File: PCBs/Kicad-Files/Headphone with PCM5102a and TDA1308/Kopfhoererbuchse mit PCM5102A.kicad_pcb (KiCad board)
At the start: 2 copper layers, 30.9 x 31.3 mm, 36 parts, among them J1 Conn_02x03_Odd_Even, J2 AudioJack3_Dual_Switch, Q1 IRLML6401, U1 PCM5102A, U2 TDA1308

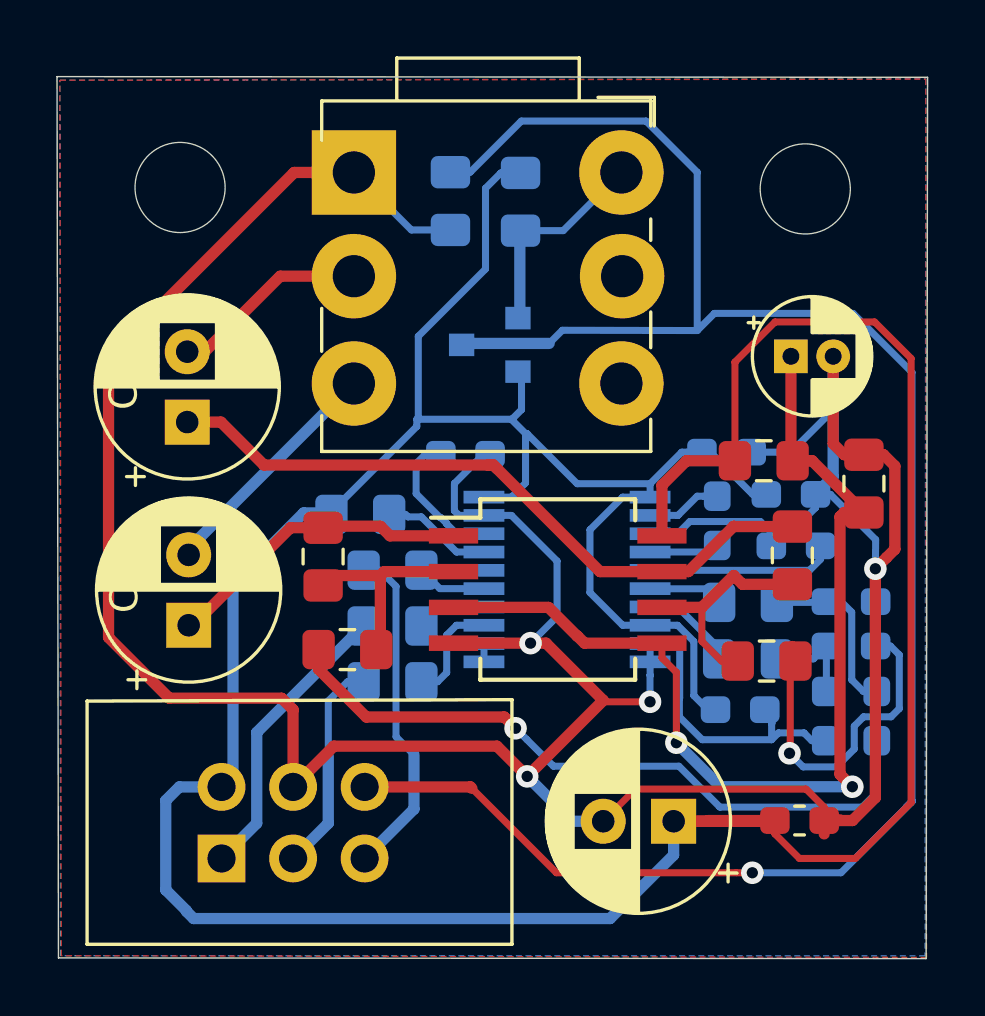
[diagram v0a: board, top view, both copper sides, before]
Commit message: KiCad-Files umbenennen: Kopfhoererplatine
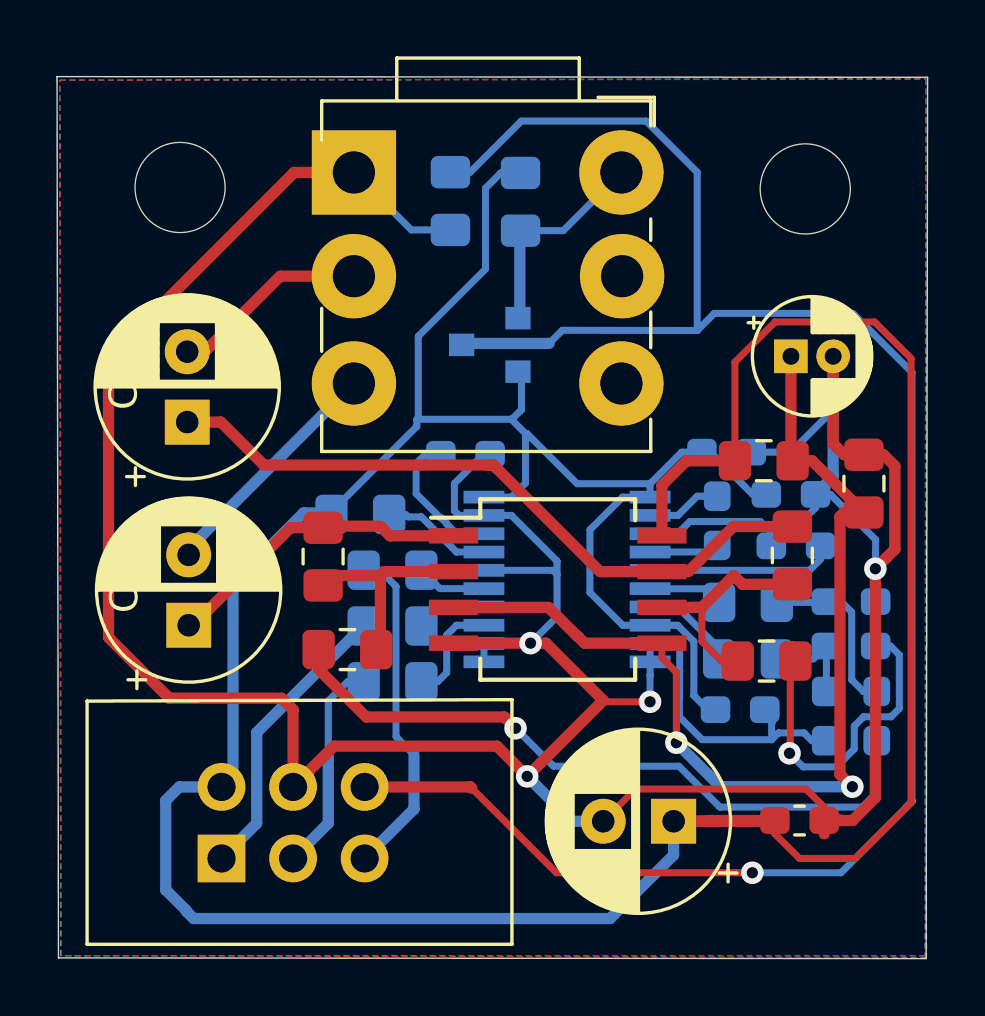
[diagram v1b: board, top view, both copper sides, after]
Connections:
- U1 pad 16: (no net) -> GND
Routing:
- net GND: track 136.4 -> 139.0 mm
